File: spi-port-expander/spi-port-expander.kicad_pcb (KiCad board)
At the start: 2 copper layers, 83 x 71 mm, 56 parts, among them J1 Power_Terminal, J10 Screw_Terminal_01x02, J11 Screw_Terminal_01x02, J12 Screw_Terminal_01x02, J2 Conn_01x19_Pin, J3 Power_Terminal, J4 Conn_01x19_Socket, J5 Power_Terminal, J6 Conn_01x19_Socket, J7 Conn_01x19_Pin, J8 Power_Terminal, J9 Screw_Terminal_01x02, U1 LM7805, U2 IXDD604PI, U3 IXDD604PI, U4 IXDD604PI, U5 IXDD604PI

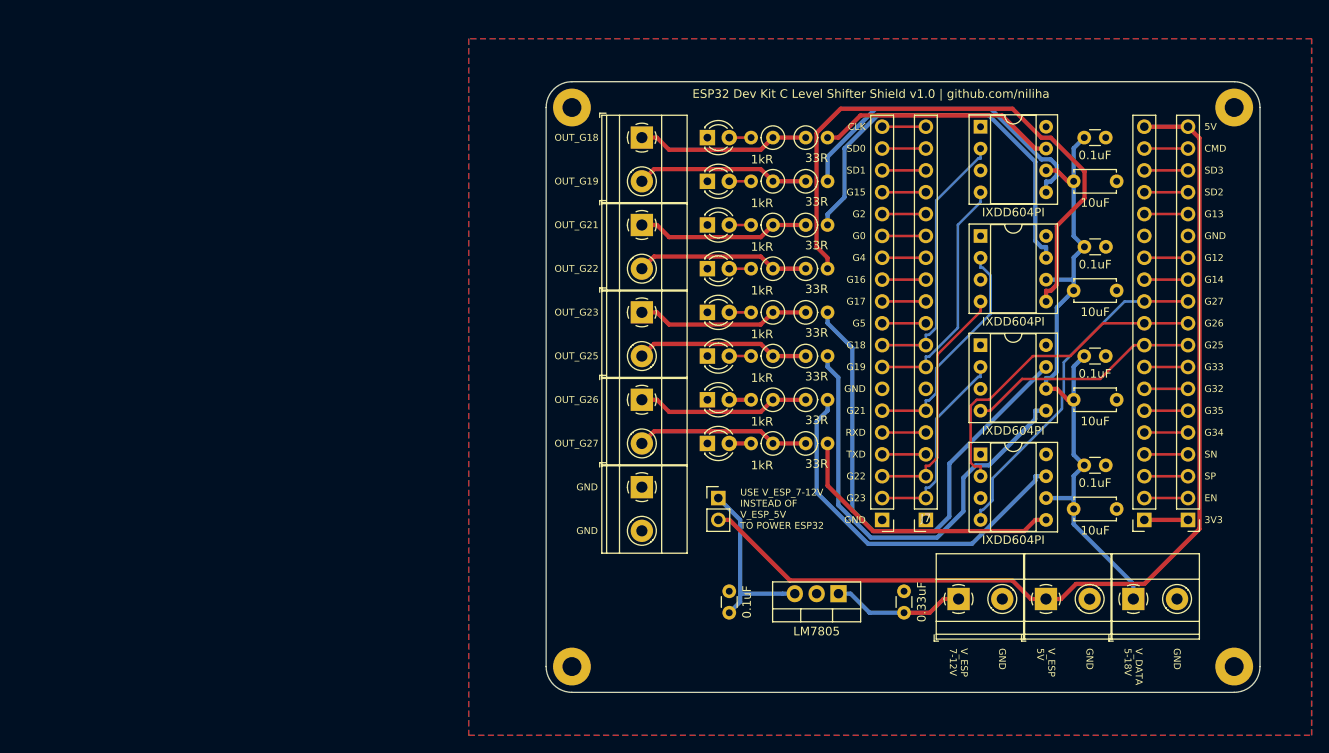
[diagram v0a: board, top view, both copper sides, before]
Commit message: Finish SPI port expander layout
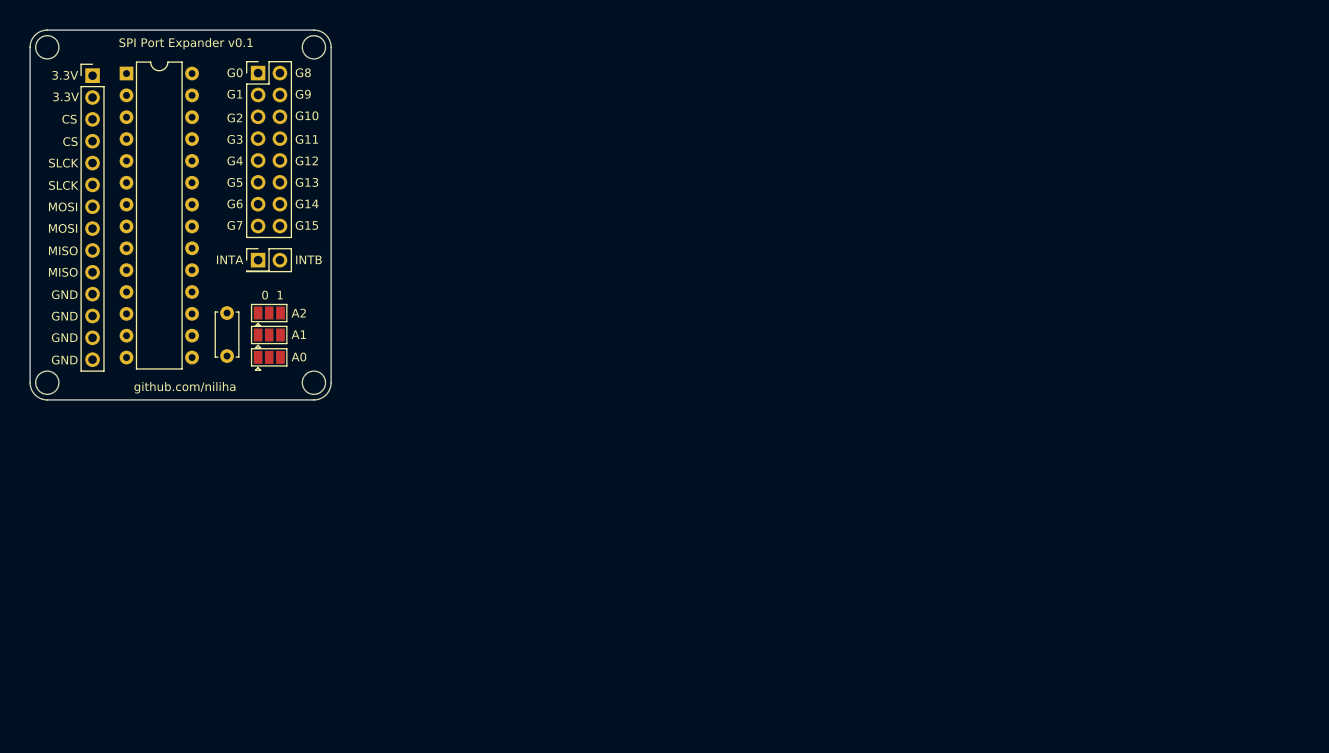
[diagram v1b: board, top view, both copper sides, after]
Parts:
- removed C10, C7, C8, C9: 10uF, Capacitor_THT:C_Disc_D4.7mm_W2.5mm_P5.00mm
- removed C2, C3, C4, C5, C6: 0.1uF, Capacitor_THT:C_Disc_D3.0mm_W1.6mm_P2.50mm
- removed D1, D2, D3, D4, D5, D6, D7, D8: RED, LED_THT:LED_D3.0mm
- removed J10, J11, J12, J9: Screw_Terminal_01x02, TerminalBlock_Phoenix:TerminalBlock_Phoenix_MKDS-1,5-2-5.08_1x02_P5.08mm_Horizontal
- removed J2, J7: Conn_01x19_Pin, Connector_PinHeader_2.54mm:PinHeader_1x19_P2.54mm_Vertical
- removed J5, J8: Power_Terminal, TerminalBlock_Phoenix:TerminalBlock_Phoenix_MKDS-1,5-2-5.08_1x02_P5.08mm_Horizontal
- removed J6: Conn_01x19_Socket, Connector_PinSocket_2.54mm:PinSocket_1x19_P2.54mm_Vertical
- removed R1, R2, R3, R4, R5, R6, R7, R8: 33R, Resistor_THT:R_Axial_DIN0207_L6.3mm_D2.5mm_P2.54mm_Vertical
- removed R10, R11, R12, R13, R14, R15, R16, R9: 1kR, Resistor_THT:R_Axial_DIN0207_L6.3mm_D2.5mm_P2.54mm_Vertical
- removed U2, U3, U4, U5: IXDD604PI, Package_DIP:DIP-8_W7.62mm_Socket
- added JP2: SolderJumper_3_Open, Jumper:SolderJumper-3_P1.3mm_Open_Pad1.0x1.5mm, F.Cu at (107.8, 86.5)
- added JP3: SolderJumper_3_Open, Jumper:SolderJumper-3_P1.3mm_Open_Pad1.0x1.5mm, F.Cu at (107.8, 89.0)
- C1: value 0.33uF -> 0.1uF; footprint Capacitor_THT:C_Disc_D3.0mm_W1.6mm_P2.50mm -> Capacitor_THT:C_Disc_D5.0mm_W2.5mm_P5.00mm
- H1, H2, H3, H4: footprint MountingHole:MountingHole_2.2mm_M2_Pad -> MountingHole:MountingHole_2.7mm_M2.5
- J1: value Power_Terminal -> Conn_01x14_Pin; footprint TerminalBlock_Phoenix:TerminalBlock_Phoenix_MKDS-1,5-2-5.08_1x02_P5.08mm_Horizontal -> Connector_PinHeader_2.54mm:PinHeader_1x14_P2.54mm_Vertical
- J3: value Power_Terminal -> Conn_02x01; footprint TerminalBlock_Phoenix:TerminalBlock_Phoenix_MKDS-1,5-2-5.08_1x02_P5.08mm_Horizontal -> Connector_PinHeader_2.54mm:PinHeader_2x01_P2.54mm_Vertical
- J4: value Conn_01x19_Socket -> Conn_02x08_Odd_Even; footprint Connector_PinSocket_2.54mm:PinSocket_1x19_P2.54mm_Vertical -> Connector_PinHeader_2.54mm:PinHeader_2x08_P2.54mm_Vertical
- JP1: value Jumper_2_Open -> SolderJumper_3_Open; footprint Connector_PinHeader_2.54mm:PinHeader_1x02_P2.54mm_Vertical -> Jumper:SolderJumper-3_P1.3mm_Open_Pad1.0x1.5mm
- U1: value LM7805 -> MCP23S17_SP; footprint Package_TO_SOT_THT:TO-220-3_Vertical -> Package_DIP:DIP-28_W7.62mm
- moved J1 135.5 mm to (87.3, 56.3)
- moved J4 115.4 mm to (106.5, 56.0), turned to 0 degrees
- moved H3 112.0 mm to (113.0, 92.0)
- moved H2 107.2 mm to (113.0, 53.0)
- moved U1 102.5 mm to (91.2, 56.0), turned to 0 degrees
- moved J3 99.7 mm to (106.5, 77.8)
- moved C1 86.1 mm to (102.9, 83.9), turned to -90 degrees
- moved H4 69.4 mm to (82.0, 92.0)
- moved H1 61.4 mm to (82.0, 53.0)
- moved JP1 56.5 mm to (107.8, 83.9)
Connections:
- C1 pad 1: V_ESP_7-12V -> +3.3V
- J1 pad 1: V_DATA -> +3.3V
- J1 pad 2: GND -> +3.3V
- J3 pad 1: V_ESP_5V -> INTA
- J3 pad 2: GND -> INTB
- J4 pad 1: /3V3 -> G0
- J4 pad 10: /G26 -> G12
- J4 pad 11: /G27 -> G5
- J4 pad 12: /G14 -> G13
- J4 pad 13: /G12 -> G6
- J4 pad 14: GND -> G14
- J4 pad 15: /G13 -> G7
- J4 pad 16: /SD2 -> G15
- J4 pad 2: /EN -> G8
- J4 pad 3: /SP -> G1
- J4 pad 4: /SN -> G9
- J4 pad 5: /G34 -> G2
- J4 pad 6: /G35 -> G10
- J4 pad 7: /G32 -> G3
- J4 pad 8: /G33 -> G11
- J4 pad 9: /G25 -> G4
- JP1 pad 1: /5V_OUT_REG -> GND
- JP1 pad 2: V_ESP_5V -> A2
- U1 pad 1: V_ESP_7-12V -> G8
- U1 pad 2: GND -> G9
- U1 pad 3: /5V_OUT_REG -> G10
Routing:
- net V_ESP_5V: track 115.5 -> 0.00 mm
- net V_DATA: track 78.9 -> 0.00 mm
- net /OUT_G22: track 69.0 -> 0.00 mm
- net /OUT_G23: track 59.2 -> 0.00 mm
- net /OUT_G25: track 52.5 -> 0.00 mm
- net /OUT_G21: track 47.7 -> 0.00 mm
- net /OUT_G26: track 44.0 -> 0.00 mm
- net /G27: track 39.9 -> 0.00 mm
- net /OUT_G19: track 38.5 -> 0.00 mm
- net /G26: track 38.3 -> 0.00 mm
- net /OUT_G27: track 33.0 -> 0.00 mm
- net /G18: track 30.9 -> 0.00 mm
- net /G19: track 28.2 -> 0.00 mm
- net /G22: track 28.2 -> 0.00 mm
- net /OUT_G18: track 28.1 -> 0.00 mm
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- removed copper zone on B.Cu, net GND
- removed copper zone on F.Cu, net GND
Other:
- board size 83 x 71 mm -> 35 x 43 mm
- board text added: "0 1"
- board text added: "3.3V"
- board text added: "A0"
- board text added: "A1"
- board text added: "A2"
- board text added: "CS"
- board text added: "G1"
- board text added: "G10"
- board text added: "G11"
- board text added: "G3"
- board text added: "G6"
- board text added: "G7"
- board text added: "G8"
- board text added: "G9"
- board text added: "INTA"
- board text added: "INTB"
- board text added: "MISO"
- board text added: "MOSI"
- board text added: "SLCK"
- board text added: "SPI Port Expander v0.1"
- board text added: "github.com/niliha"
- board text removed: "3V3"
- board text removed: "5V"
- board text removed: "CLK"
- board text removed: "CMD"
- board text removed: "EN"
- board text removed: "ESP32 Dev Kit C Level Shifter Shield v1.0 | github.com/niliha"
- board text removed: "G16"
- board text removed: "G17"
- board text removed: "G18"
- board text removed: "G19"
- board text removed: "G21"
- board text removed: "G22"
- board text removed: "G23"
- board text removed: "G25"
- board text removed: "G26"
- board text removed: "G27"
- board text removed: "G32"
- board text removed: "G33"
- board text removed: "G34"
- board text removed: "G35"
- board text removed: "OUT_G18"
- board text removed: "OUT_G19"
- board text removed: "OUT_G21"
- board text removed: "OUT_G22"
- board text removed: "OUT_G23"
- board text removed: "OUT_G25"
- board text removed: "OUT_G26"
- board text removed: "OUT_G27"
- board text removed: "RXD"
- board text removed: "SD0"
- board text removed: "SD1"
- board text removed: "SD2"
- board text removed: "SD3"
- board text removed: "SN"
- board text removed: "SP"
- board text removed: "TXD"
- board text removed: "USE V_ESP_7-12V INSTEAD OF V_ESP_5V TO POWER ESP32"
- board text removed: "V_DATA 5-18V"
- board text removed: "V_ESP 5V"
- board text removed: "V_ESP 7-12V"

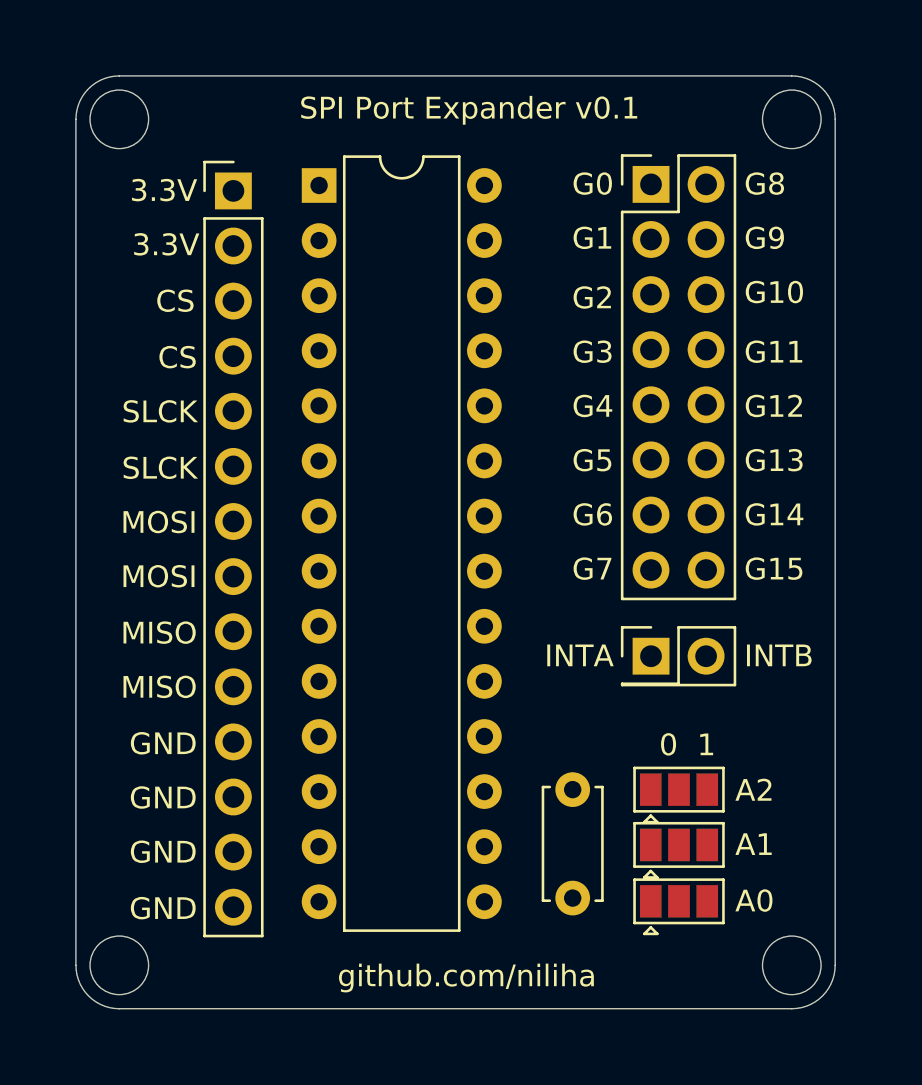
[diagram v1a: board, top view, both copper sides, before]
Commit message: Create production files for SPI port expander
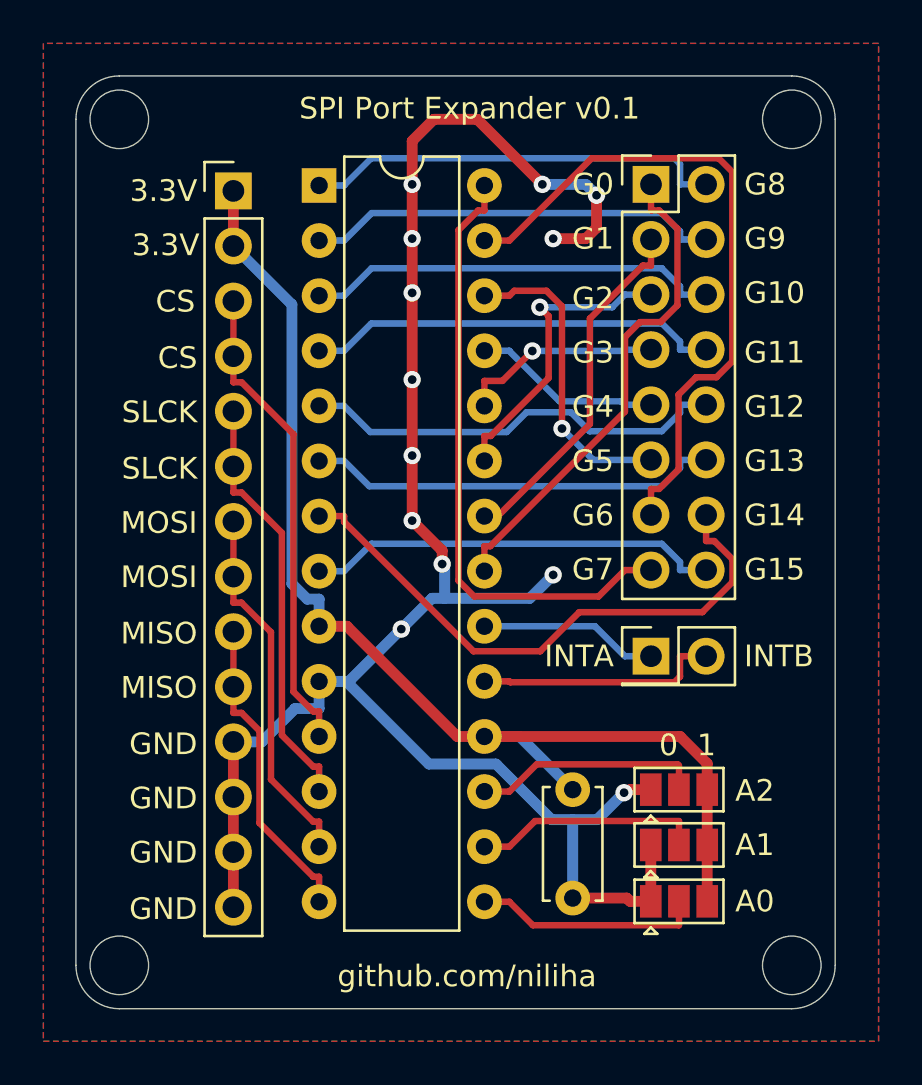
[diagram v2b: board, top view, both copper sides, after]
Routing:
- net GND: track 0.00 -> 90.4 mm, vias 0 -> 13
- net +3.3V: track 0.00 -> 54.0 mm
- net G6: track 0.00 -> 31.4 mm
- net G7: track 0.00 -> 28.6 mm
- net G14: track 0.00 -> 26.9 mm
- net G0: track 0.00 -> 23.0 mm
- net CS: track 0.00 -> 22.1 mm
- net G12: track 0.00 -> 19.8 mm
- net SLCK: track 0.00 -> 19.5 mm
- net G8: track 0.00 -> 19.4 mm
- net G9: track 0.00 -> 19.1 mm
- net G10: track 0.00 -> 19.1 mm
- net G15: track 0.00 -> 19.1 mm
- net G11: track 0.00 -> 19.1 mm
- net G13: track 0.00 -> 19.0 mm
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- added copper zone on B.Cu, net GND
- added copper zone on F.Cu, net GND
